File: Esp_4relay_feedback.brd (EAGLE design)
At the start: 130 x 95 mm, 77 parts, among them IC1 LM1117MP-3.3, IC4 7805TV, K1 G5LE, K2 G5LE, K3 G5LE, K4 G5LE, K5 G5LE, K6 G5LE, K7 G5LE, K8 G5LE, Q1 16MHz, Q2 BC547, Q3 BC547, Q4 BC547, Q5 BC547, Q6 BC547, Q7 BC547, Q8 BC547, Q9 BC547, U2 ATMEGA328P_PDIP

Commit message: pdf added
added
bottom layer pdf
top layer pdf
both side pdf
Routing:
- net N$23: track 88.0 -> 0.00 mm
- added copper zone on layer 1, net GND1
- added copper zone on layer 16, net N$23
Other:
- board size 130 x 95 mm -> 150 x 100 mm
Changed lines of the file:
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@@
 <setting verticaltext="up"/>
 </settings>
-<grid distance="1" unitdist="mil" unit="mil" style="lines" multiple="1" display="yes" altdistance="1" altunitdist="mm" altunit="mm"/>
+<grid distance="1" unitdist="mm" unit="mm" style="lines" multiple="1" display="yes" altdistance="1" altunitdist="mm" altunit="mm"/>
 <layers>
 <layer number="1" name="Top" color="4" fill="1" visible="yes" active="yes"/>
@@
 <layer number="14" name="Route14" color="1" fill="6" visible="no" active="no"/>
 <layer number="15" name="Route15" color="4" fill="6" visible="no" active="no"/>
-<layer number="16" name="Bottom" color="1" fill="1" visible="yes" active="yes"/>
+<layer number="16" name="Bottom" color="1" fill="1" visible="no" active="yes"/>
 <layer number="17" name="Pads" color="2" fill="1" visible="yes" active="yes"/>
 <layer number="18" name="Vias" color="2" fill="1" visible="yes" active="yes"/>
-<layer number="19" name="Unrouted" color="6" fill="1" visible="yes" active="yes"/>
+<layer number="19" name="Unrouted" color="6" fill="1" visible="no" active="yes"/>
 <layer number="20" name="Dimension" color="15" fill="1" visible="yes" active="yes"/>
-<layer number="21" name="tPlace" color="7" fill="1" visible="yes" active="yes"/>
+<layer number="21" name="tPlace" color="7" fill="1" visible="no" active="yes"/>
 <layer number="22" name="bPlace" color="7" fill="1" visible="no" active="yes"/>
-<layer number="23" name="tOrigins" color="15" fill="1" visible="yes" active="yes"/>
+<layer number="23" name="tOrigins" color="15" fill="1" visible="no" active="yes"/>
 <layer number="24" name="bOrigins" color="15" fill="1" visible="no" active="yes"/>
-<layer number="25" name="tNames" color="7" fill="1" visible="yes" active="yes"/>
+<layer number="25" name="tNames" color="7" fill="1" visible="no" active="yes"/>
 <layer number="26" name="bNames" color="7" fill="1" visible="no" active="yes"/>
 <layer number="27" name="tValues" color="7" fill="1" visible="no" active="yes"/>
@@
 <board>
 <plain>
-<wire x1="104" y1="2" x2="234" y2="2" width="0" layer="20"/>
-<wire x1="234" y1="2" x2="234" y2="97" width="0" layer="20"/>
-<wire x1="234" y1="97" x2="104" y2="97" width="0" layer="20"/>
-<wire x1="104" y1="97" x2="104" y2="2" width="0" layer="20"/>
+<wire x1="96" y1="0" x2="246" y2="0" width="0" layer="20"/>
+<wire x1="246" y1="0" x2="246" y2="100" width="0" layer="20"/>
+<wire x1="246" y1="100" x2="96" y2="100" width="0" layer="20"/>
+<wire x1="96" y1="100" x2="96" y2="0" width="0" layer="20"/>
 <circle x="108" y="93" radius="2" width="0.254" layer="20"/>
 <circle x="230" y="93" radius="2" width="0.254" layer="20"/>
 <circle x="230" y="6" radius="2" width="0.254" layer="20"/>
 <circle x="108" y="6" radius="2" width="0.254" layer="20"/>
-<dimension x1="104" y1="2" x2="234" y2="2" x3="169" y3="-9" layer="1"/>
-<dimension x1="234" y1="2" x2="234" y2="97" x3="244" y3="49.5" layer="1"/>
-<dimension x1="125" y1="-2" x2="213" y2="-2" x3="169" y3="-2" layer="1"/>
 </plain>
 <attributes>
@@
 </signal>
 <signal name="N$23">
-<wire x1="125" y1="-2" x2="213" y2="-2" width="0.8128" layer="1"/>
+<polygon width="0.6096" layer="16" isolate="2.54">
+<vertex x="97" y="100"/>
+<vertex x="246" y="100"/>
+<vertex x="246" y="0"/>
+<vertex x="96" y="0"/>
+<vertex x="96" y="100"/>
+</polygon>
+</signal>
+<signal name="GND1">
+<polygon width="0.6096" layer="1" isolate="2.1844">
+<vertex x="96" y="100"/>
+<vertex x="246" y="100"/>
+<vertex x="246" y="0"/>
+<vertex x="96" y="0"/>
+</polygon>
 </signal>
 </signals>

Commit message: polygon added.
polygon added.
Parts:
- R11, R12, R4: value (none) -> 10k

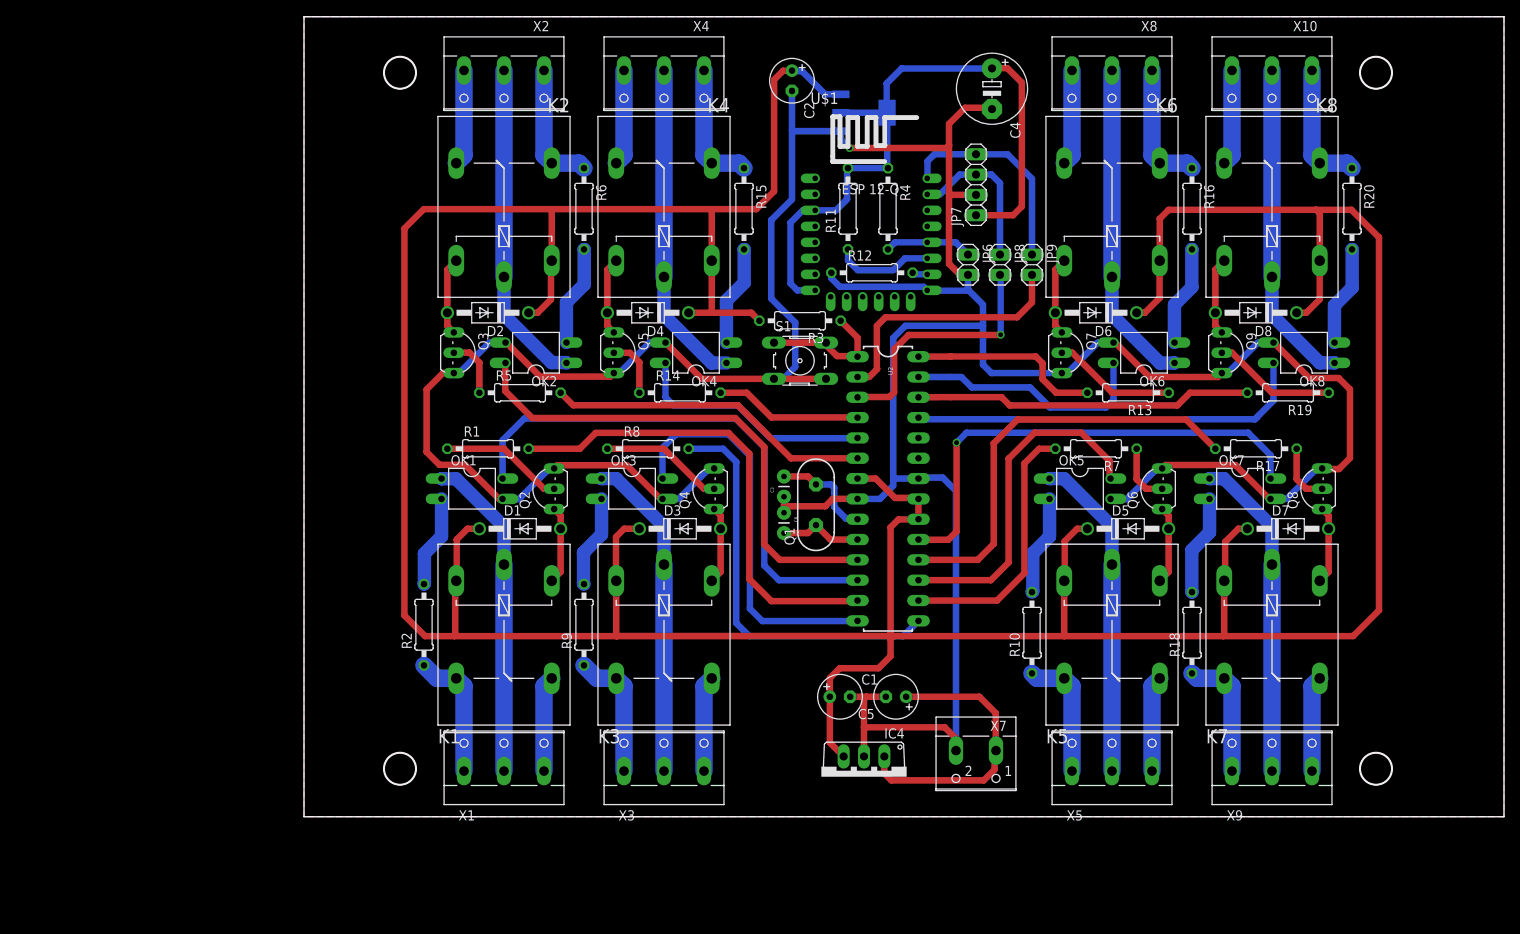
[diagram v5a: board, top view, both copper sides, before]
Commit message: feature added
added power on delay for relay supply.
added logic level for esp to atmega328 communication.
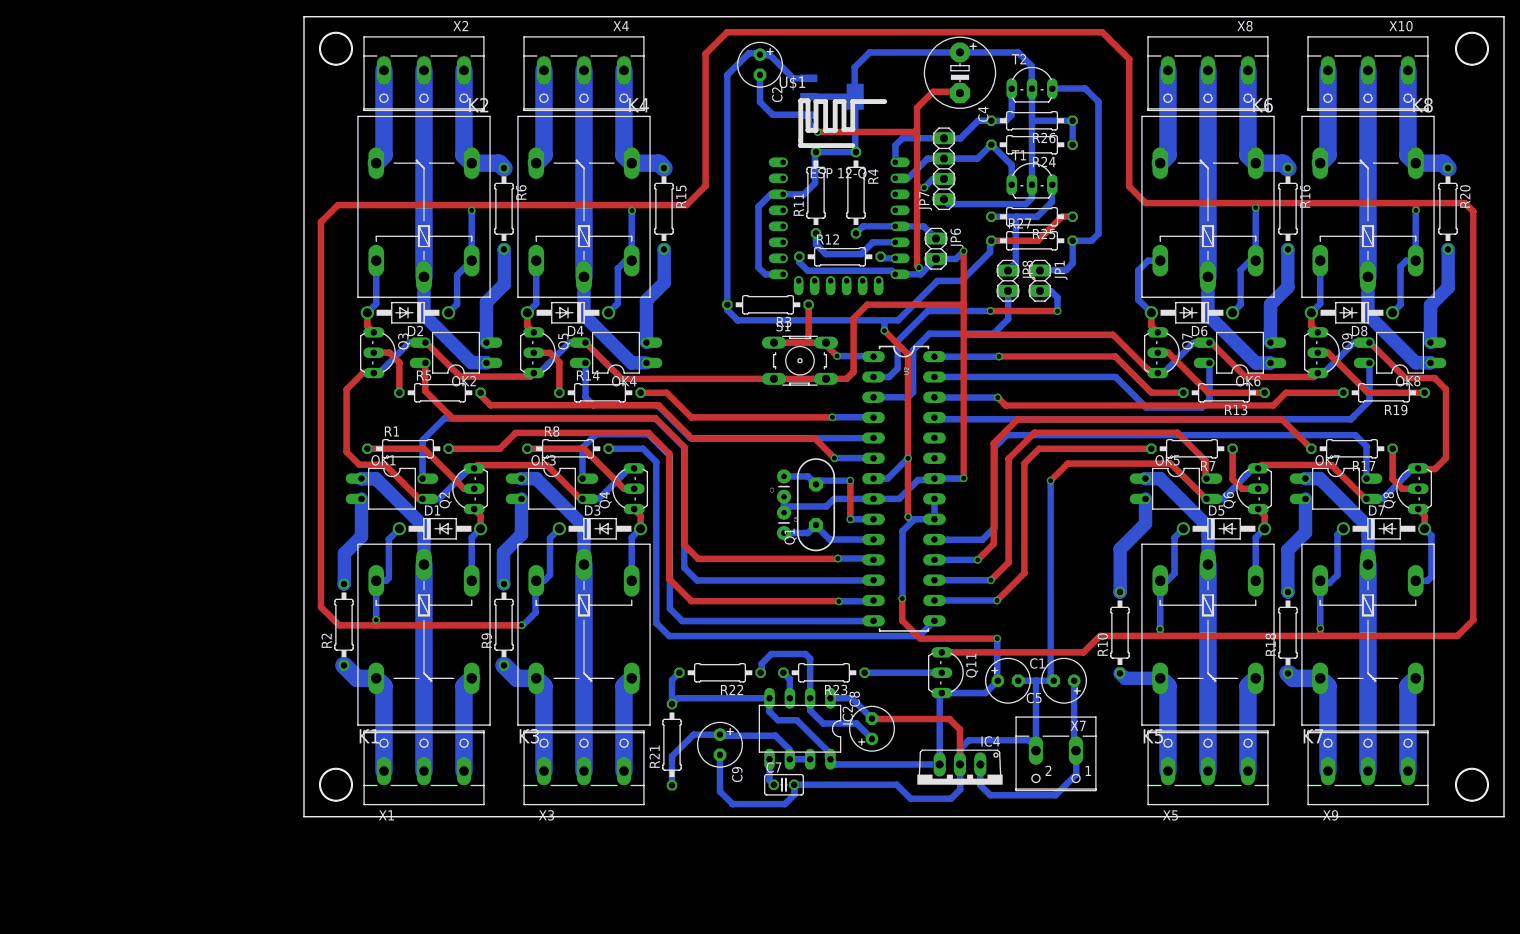
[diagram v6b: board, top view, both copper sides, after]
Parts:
- removed JP9: (no value), pinhead:1X02
- added C7: 0.01uf, rcl:C025-025X050
- added C8: 10uf, rcl:E2,5-6
- added C9: 100uf, rcl:E2,5-6
- added IC2: NE555, st-microelectronics:DIL-08
- added JP1: (no value), pinhead:1X02
- added Q11: BC450, transistor-pnp:TO92-EBC
- added R21: 47k, rcl:0207/10
- added R22, R23: 1k, rcl:0207/10
- added R24, R25, R26, R27: 10k, rcl:0207/10
- added T1, T2: 2N7000, transistor:TO92-CBE
- moved C1 21.1 mm to (184.0, 17.0)
- moved C5 21.1 mm to (191.0, 17.0)
- moved IC4 12.0 mm to (178.0, 4.00)
- moved D5 12.0 mm to (211.0, 36.0)
- moved D6 12.0 mm to (207.0, 63.0)
- moved D7 12.0 mm to (231.0, 36.0)
- moved D8 12.0 mm to (227.0, 63.0)
- moved K5 12.0 mm to (209.0, 22.0)
- moved K6 12.0 mm to (209.0, 77.0)
- moved K7 12.0 mm to (229.0, 22.0)
- moved K8 12.0 mm to (229.0, 77.0)
- moved OK5 12.0 mm to (205.0, 41.0)
- moved OK6 12.0 mm to (213.0, 58.0)
- moved OK7 12.0 mm to (225.0, 41.0)
- moved OK8 12.0 mm to (233.0, 58.0)
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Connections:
- new net N$23: JP1.1, R27.2, T2.E
- new net N$26: C9.+, IC2.6, IC2.7, R21.1
- new net N$27: JP8.1, R25.2, T1.E
- new net N$36: C8.+, IC2.2, R22.1
- new net N$37: C7.1, IC2.5
- new net N$38: IC2.3, R23.2
- new net N$39: Q11.B, R23.1
- new net RELAY_SUPPLY: D1.C, D2.C, D3.C, D4.C, D5.C, D6.C, D7.C, D8.C, K1.1, K2.1, K3.1, K4.1, K5.1, K6.1, K7.1, K8.1, Q11.C
- net 3V3: now also R24.1, R26.1, T1.B, T2.B
- net GND: now also C7.2, C8.-, C9.-, IC2.1
- net RX: now also JP1.2; no longer JP9.2
- net RX1: now also R24.2, T1.C; no longer JP8.1
- net TX1: now also R26.2, T2.C; no longer JP9.1
- net VCC: now also IC2.4, IC2.8, Q11.E, R21.2, R22.2, R25.1, R27.1; no longer D1.C, D2.C, D3.C, D4.C, D5.C, D6.C, D7.C, D8.C, K1.1, K2.1, K3.1, K4.1, K5.1, K6.1, K7.1, K8.1
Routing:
- net RELAY_SUPPLY: track 0.00 -> 496.0 mm, vias 0 -> 8
- net VCC: track 499.1 -> 220.0 mm, vias 0 -> 5
- net GND: track 443.0 -> 528.7 mm, vias 4 -> 9
- net N$23: track 0.00 -> 33.9 mm
- net N$26: track 0.00 -> 24.0 mm
- net N$36: track 0.00 -> 23.6 mm
- net 3V3: track 84.8 -> 104.8 mm
- net N$27: track 0.00 -> 17.7 mm
- net R2: track 40.5 -> 52.7 mm, vias 0 -> 1
- net F1: track 67.3 -> 79.5 mm
- net F2: track 63.4 -> 75.5 mm, vias 0 -> 1
- net R1: track 59.9 -> 71.9 mm, vias 0 -> 1
- net R4: track 18.4 -> 30.4 mm, vias 0 -> 1
- net F4: track 30.4 -> 42.4 mm
- net R3: track 51.0 -> 63.0 mm
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- removed copper zone on layer 1, net GND1
- removed copper zone on layer 16, net N$23
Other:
- outline, holes or cut-outs redrawn

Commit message: Esp pull up added
pull up for reset and chpd.
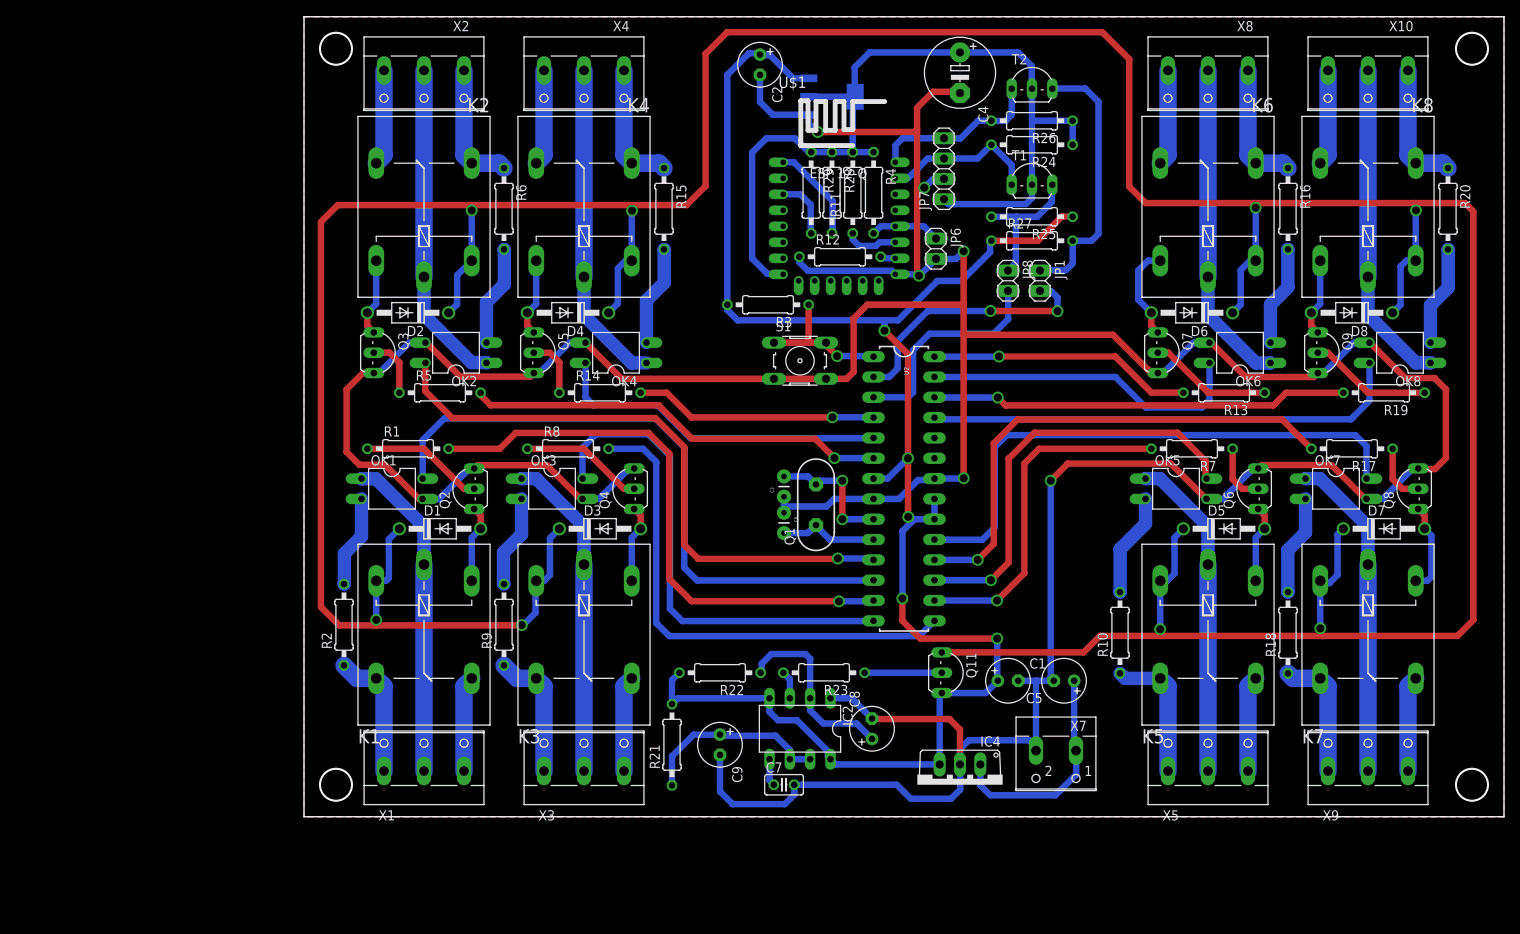
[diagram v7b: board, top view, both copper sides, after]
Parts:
- added R28, R29: 10k, rcl:0207/10
- moved R11 4.60 mm to (164.6, 78.0)
- moved R4 2.20 mm to (167.2, 78.0)
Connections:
- new net N$40: R29.2, U$1.CH_PD
- new net N$41: R28.2, U$1.RESET
- net 3V3: now also R28.1, R29.1; no longer U$1.CH_PD
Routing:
- net N$41: track 0.00 -> 12.3 mm
- net N$40: track 0.00 -> 7.58 mm
- net 3V3: track 104.8 -> 111.2 mm
- net N$21: track 12.4 -> 6.59 mm
- net IO0: track 11.0 -> 8.80 mm
- added copper zone on layer 16, net N$42
- added copper zone on layer 1, net N$43

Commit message: pad removed from top side
top side pad overlaped with vias,
top side pdf contains only tracks n vias.
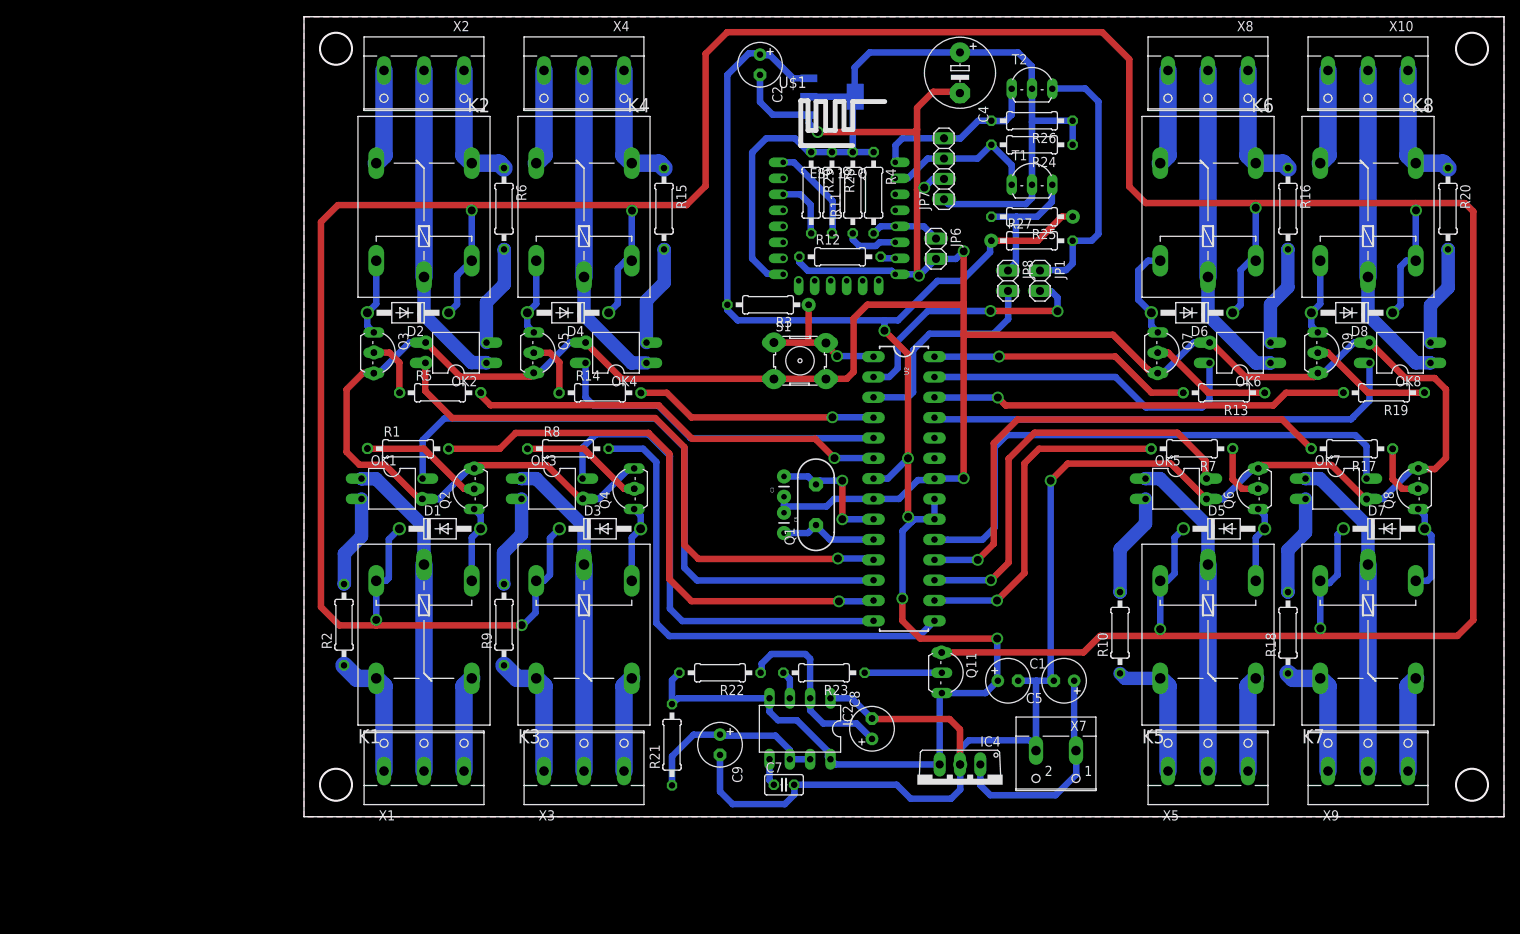
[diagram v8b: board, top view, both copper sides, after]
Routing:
- net N$55: vias 0 -> 1
- net N$35: vias 0 -> 1
- net GND: vias 9 -> 10
